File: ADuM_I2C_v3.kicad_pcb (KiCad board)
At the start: 4 copper layers, 42 parts, among them J1 A, J2 B, Q1 BSS138, Q2 BSS138, Q3 BSS138, Q4 BSS138, Q5 BSS138, Q6 BSS138, Q7 BSS138, Q8 BSS138, U1 ADuM1251ARZ, U2 ADuM1201AR

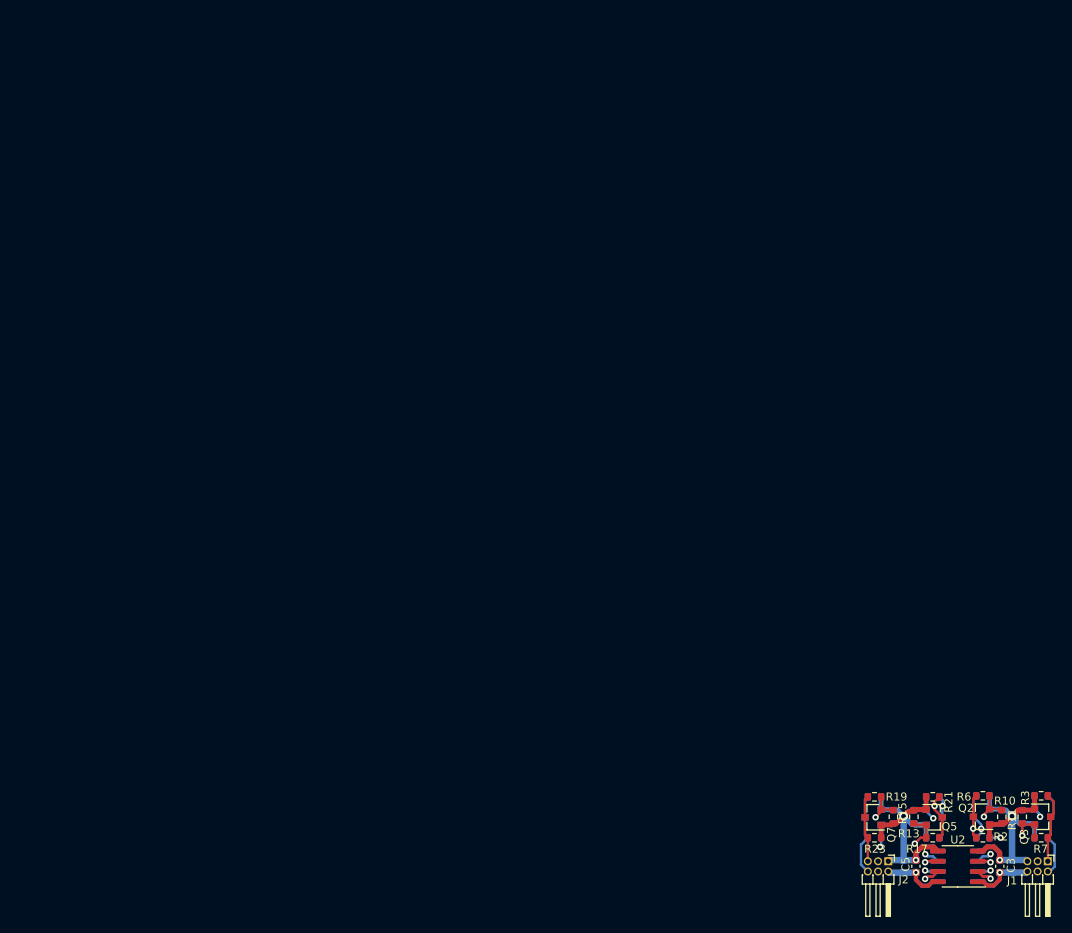
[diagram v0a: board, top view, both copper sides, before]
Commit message: Переделана панелизация платы ADuM_I2C_v3
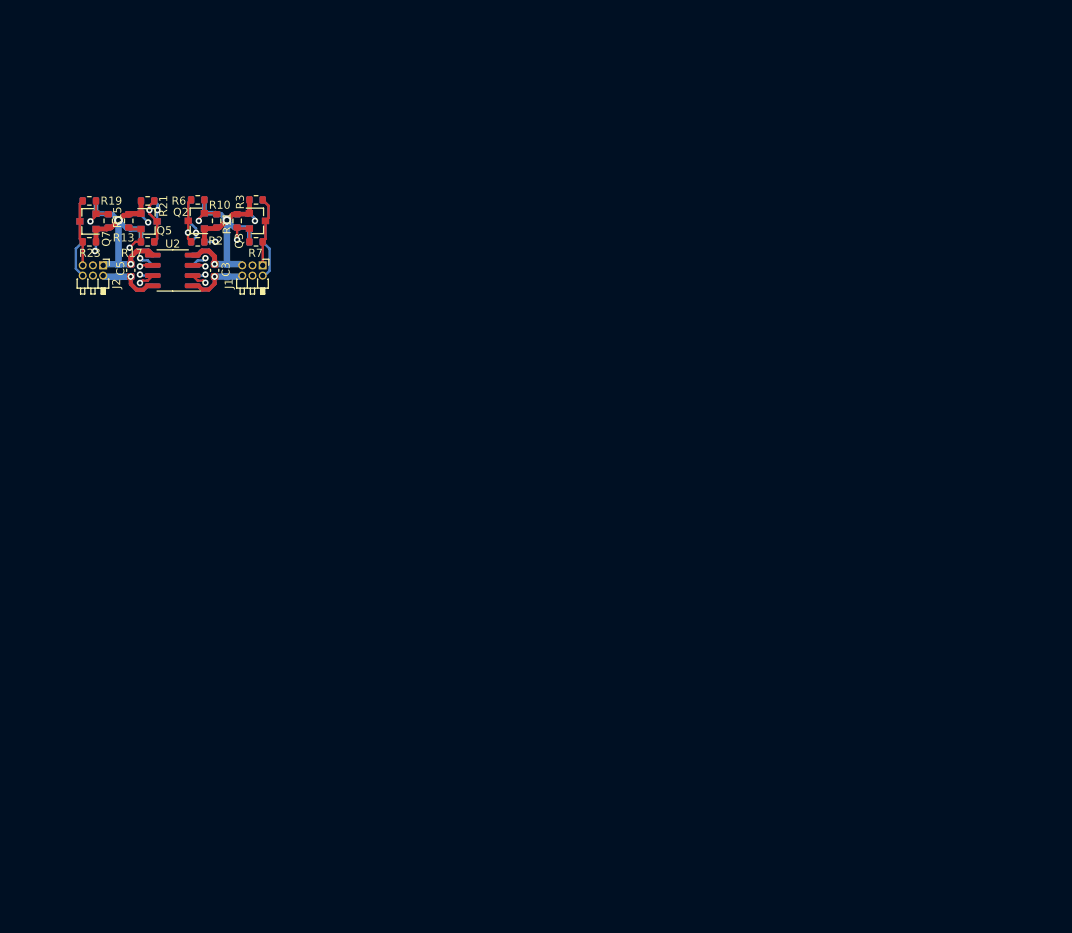
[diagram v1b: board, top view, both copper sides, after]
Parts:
- J1, J2: footprint Connector_PinHeader_1.27mm:PinHeader_2x03_P1.27mm_Horizontal -> Modules:PinHeader_2x03_P1.27mm_Horizontal_short
- moved R9 122.4 mm to (84.5, 64.9)
- moved C6 122.4 mm to (72.3, 71.1)
- moved Q1 122.4 mm to (81.9, 64.9)
- moved Q2 122.4 mm to (81.9, 64.9)
- moved R10 122.4 mm to (84.5, 64.9)
- moved R16 122.4 mm to (71.0, 64.9)
- moved R18 122.4 mm to (75.9, 62.4)
- moved R19 122.4 mm to (68.6, 62.4)
- moved R21 122.4 mm to (75.9, 62.4)
- moved R24 122.4 mm to (68.7, 62.4)
- moved U1 122.4 mm to (79.0, 71.1)
- moved U2 122.4 mm to (79.0, 71.1)
- moved Q5 122.4 mm to (76.1, 65.0)
- moved Q6 122.4 mm to (76.1, 65.0)
- moved R13 122.4 mm to (73.5, 64.9)
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
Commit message: Последние изменения в BOM
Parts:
- added REF**: MountingHole_D1.524mm, Modules:MountingHole_D1.524mm, F.Cu at (71.7, 48.1)
- added REF**: MountingHole_D1.524mm, Modules:MountingHole_D1.524mm, F.Cu at (71.7, 50.4)
- moved C4 23.0 mm to (66.5, 49.2)
- moved C5 23.0 mm to (66.5, 49.2)
- moved J2 23.0 mm to (63.1, 48.6)
- moved R11 23.0 mm to (79.7, 43.1)
- moved R12 23.0 mm to (79.7, 43.1)
- moved C1 23.0 mm to (78.5, 49.2)
- moved C2 23.0 mm to (76.9, 49.2)
- moved C3 23.0 mm to (76.9, 49.2)
- moved J1 23.0 mm to (82.9, 48.6)
- moved Q2 23.0 mm to (74.7, 43.1)
- moved Q5 23.0 mm to (68.8, 43.2)
- moved Q6 23.0 mm to (68.8, 43.2)
- moved Q7 23.0 mm to (61.2, 43.2)
- moved Q8 23.0 mm to (61.2, 43.2)
- moved R1 23.0 mm to (74.8, 40.5)
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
